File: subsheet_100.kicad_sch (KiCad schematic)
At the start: 12 parts

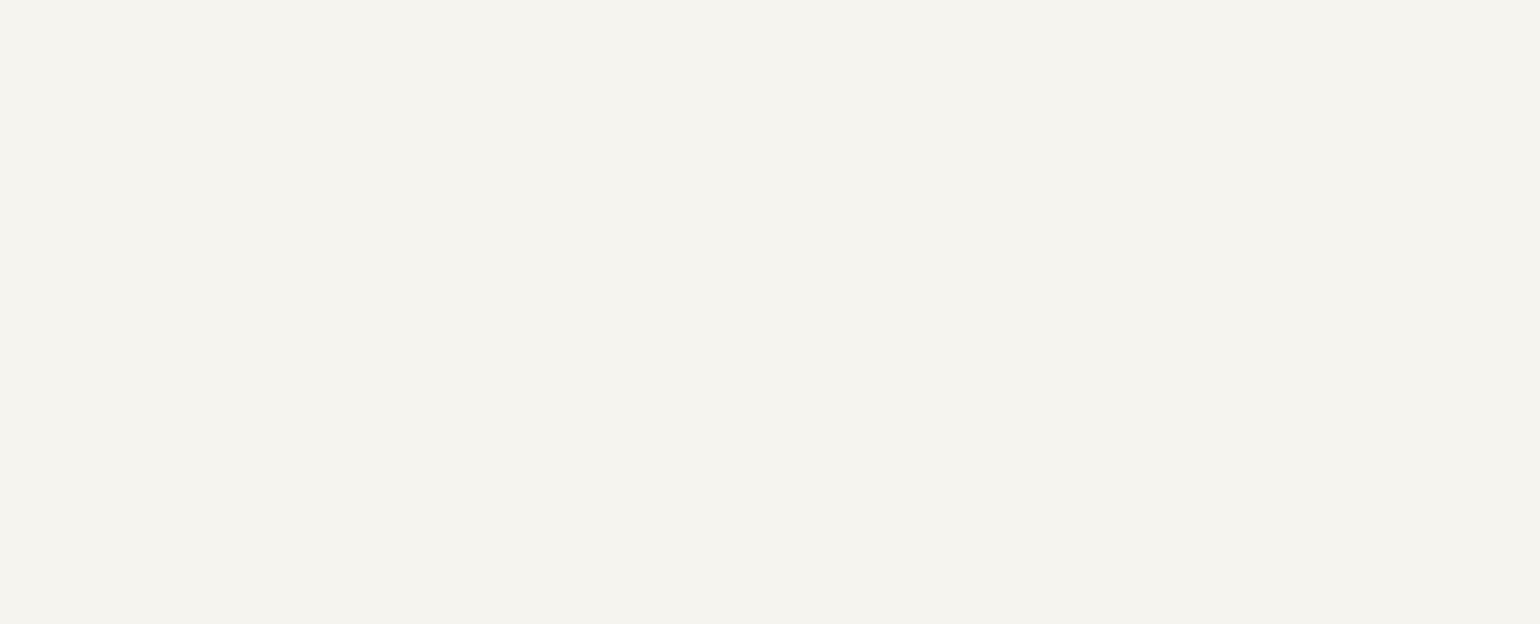
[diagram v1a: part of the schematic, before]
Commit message: bouge I21 vers la page du processeur
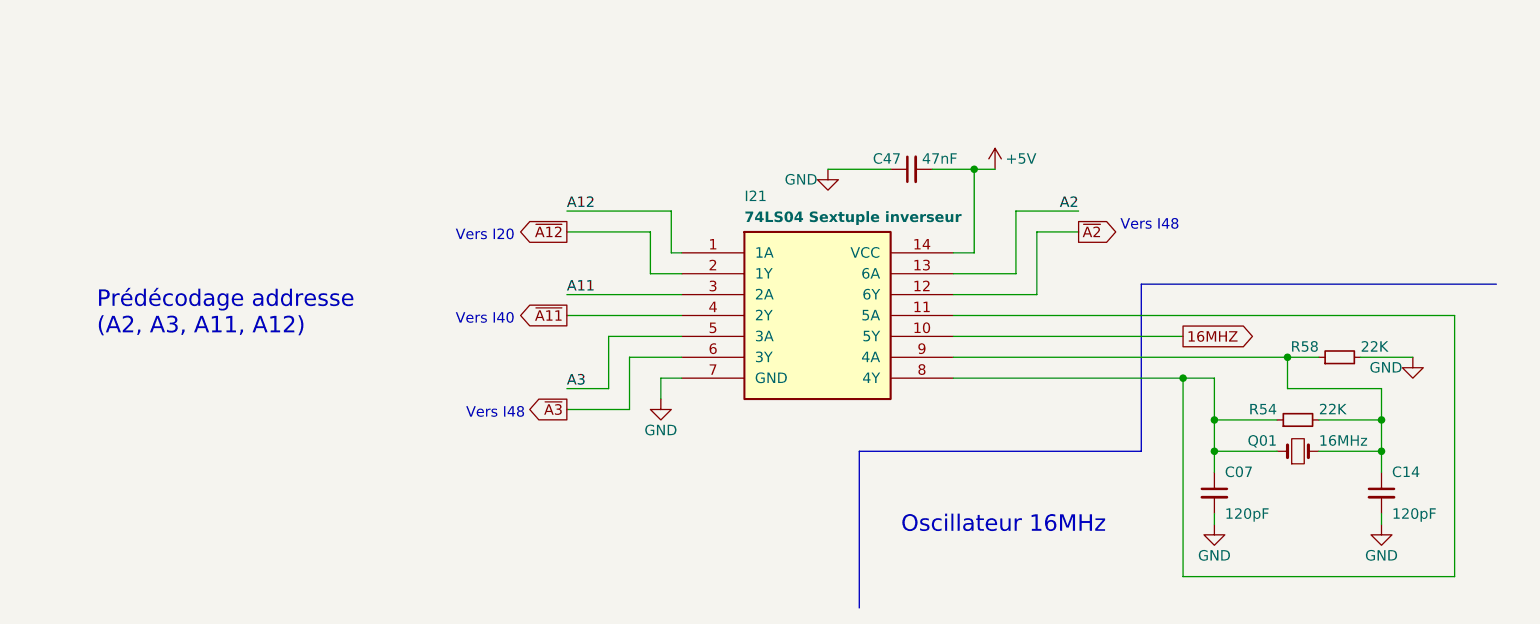
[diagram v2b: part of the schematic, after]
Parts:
- added C07, C14: 120pF, symbol Device:C_Small
- added C47: 47nF, symbol Device:C_Small
- added I21: 74LS04 Sextuple inverseur, Package_DIP:DIP-14_W7.62mm_LongPads, symbol 74x04:74X04_HEX_INVERTER_PHY
- added Q01: 16MHz, symbol Device:Crystal_Small
- added R54, R58: 22K, symbol Device:R_Small
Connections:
- net +5V: now also C47.2, I21.14 (VCC)
- net A11: now also I21.3 (2A)
- net A12: now also I21.1 (1A)
- net A2: now also I21.13 (6A)
- net A3: now also I21.5 (3A)
- net GND: now also C07.2, C14.2, C47.1, I21.7 (GND), R58.2
- new net: C07.1, I21.11 (5A), I21.8 (4Y), Q01.1, R54.1
- new net: C14.1, I21.9 (4A), Q01.2, R54.2, R58.1
- new net 16MHZ: I21.10 (5Y)
- new net ~{A11}: I21.4 (2Y)
- new net ~{A12}: I21.2 (1Y)
- new net ~{A2}: I21.12 (6Y)
- new net ~{A3}: I21.6 (3Y)
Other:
- note added: "Oscillateur 16MHz"
- note added: "Prédécodage addresse (A2, A3, A11, A12)"
- note added: "Vers I20"
- note added: "Vers I40"
- note added: "Vers I48"

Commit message: I16
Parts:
- added C44: 47nF, symbol Device:C_Small
- added I16: 74LS04 Sextuple inverseur, Package_DIP:DIP-14_W7.62mm_LongPads, symbol 74x04:74X04_HEX_INVERTER_PHY
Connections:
- net +5V: now also C44.2, I16.14 (VCC)
- net A14: now also I16.11 (5A)
- net A4: now also I16.3 (2A)
- net A5: now also I16.1 (1A)
- net GND: now also C44.1, I16.7 (GND)
- new net DATA_VALID: I16.6 (3Y)
- new net POINT: I16.12 (6Y)
- new net SYCL: I16.8 (4Y)
- new net ~{A14}: I16.10 (5Y)
- new net ~{A4}: I16.4 (2Y)
- new net ~{A5}: I16.2 (1Y)
- new net ~{DATA_VALID}: I16.5 (3A)
- new net ~{POINT}: I16.13 (6A)
- new net ~{SYCL}: I16.9 (4A)
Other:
- note added: "De I29"
- note added: "De I46"
- note added: "Prédécodage addresse (A4, A5, A14) Cadencement à contre-temps (~{DATA_VALID},~{POINT},SYCL)"
- note added: "Vers I06,I10"
- note added: "Vers I18"
- note added: "Vers I29"

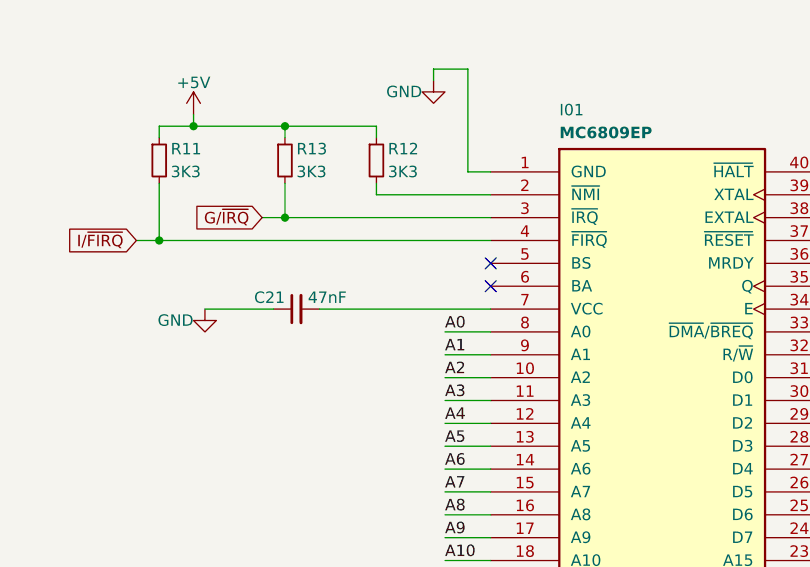
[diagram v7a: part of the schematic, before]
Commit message: fixes DRC : duplicate, designators with '?'
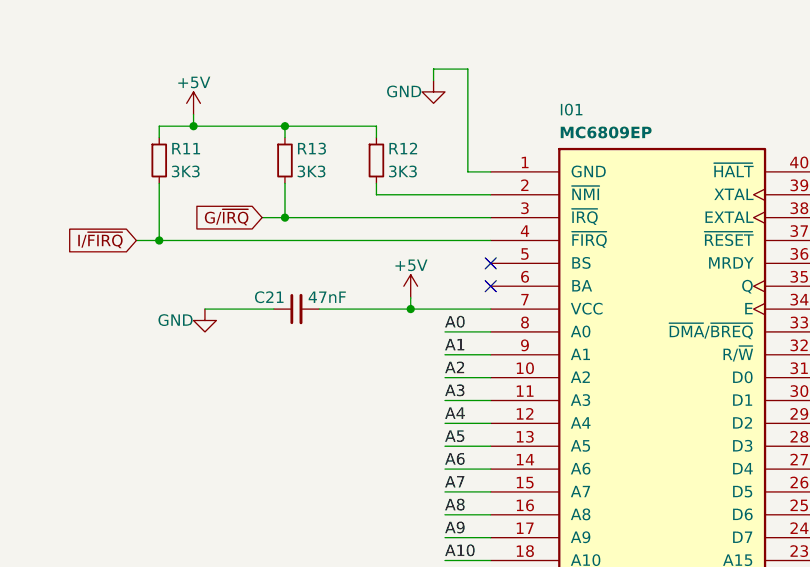
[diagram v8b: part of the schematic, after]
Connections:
- net +5V: now also C21.2, I01.7 (VCC)
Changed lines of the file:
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@@
   (junction (at 147.32 57.15) (diameter 0) (color 0 0 0 0)
+  )
+  (junction (at 58.42 64.77) (diameter 0) (color 0 0 0 0)
   )
   (junction (at 179.07 226.06) (diameter 0) (color 0 0 0 0)
@@
     (stroke (width 0) (type default) (color 0 0 0 0))
   )
+  (wire (pts (xy 58.42 64.77) (xy 67.31 64.77))
+    (stroke (width 0) (type default) (color 0 0 0 0))
+  )
   (wire (pts (xy 152.4 64.77) (xy 152.4 66.04))
     (stroke (width 0) (type default) (color 0 0 0 0))
@@
     (stroke (width 0) (type default) (color 0 0 0 0))
   )
-  (wire (pts (xy 48.26 64.77) (xy 67.31 64.77))
+  (wire (pts (xy 48.26 64.77) (xy 58.42 64.77))
     (stroke (width 0) (type default) (color 0 0 0 0))
   )
@@
   )
   (wire (pts (xy 119.38 76.2) (xy 115.57 76.2))
+    (stroke (width 0) (type default) (color 0 0 0 0))
+  )
+  (wire (pts (xy 58.42 63.5) (xy 58.42 64.77))
     (stroke (width 0) (type default) (color 0 0 0 0))
   )
@@
   (symbol (lib_id "power:+5V") (at 157.48 44.45 0) (unit 1)
     (in_bom yes) (on_board yes)
-    (property "Reference" "#PWR?" (id 0) (at 157.48 48.26 0)
+    (property "Reference" "#PWR0111" (id 0) (at 157.48 48.26 0)
       (effects (font (size 1.27 1.27)) hide)
     )
@@
   (symbol (lib_id "power:+5V") (at 132.08 132.08 0) (unit 1)
     (in_bom yes) (on_board yes)
-    (property "Reference" "#PWR?" (id 0) (at 132.08 135.89 0)
+    (property "Reference" "#PWR0106" (id 0) (at 132.08 135.89 0)
       (effects (font (size 1.27 1.27)) hide)
     )
@@
   (symbol (lib_id "power:+5V") (at 132.08 195.58 0) (unit 1)
     (in_bom yes) (on_board yes)
-    (property "Reference" "#PWR?" (id 0) (at 132.08 199.39 0)
+    (property "Reference" "#PWR0108" (id 0) (at 132.08 199.39 0)
       (effects (font (size 1.27 1.27)) hide)
     )
@@
   (symbol (lib_id "power:+5V") (at 120.65 49.53 0) (unit 1)
     (in_bom yes) (on_board yes)
-    (property "Reference" "#PWR?" (id 0) (at 120.65 53.34 0)
+    (property "Reference" "#PWR0117" (id 0) (at 120.65 53.34 0)
       (effects (font (size 1.27 1.27)) hide)
     )
@@
   (symbol (lib_id "power:GND") (at 60.96 39.37 0) (unit 1)
     (in_bom yes) (on_board yes)
-    (property "Reference" "#PWR?" (id 0) (at 60.96 45.72 0)
+    (property "Reference" "#PWR0113" (id 0) (at 60.96 45.72 0)
       (effects (font (size 1.27 1.27)) hide)
     )
@@
   (symbol (lib_id "power:GND") (at 179.07 238.76 0) (unit 1)
     (in_bom yes) (on_board yes)
-    (property "Reference" "#PWR?" (id 0) (at 179.07 245.11 0)
+    (property "Reference" "#PWR0102" (id 0) (at 179.07 245.11 0)
       (effects (font (size 1.27 1.27)) hide)
     )
@@
   (symbol (lib_id "power:GND") (at 151.13 67.31 0) (unit 1)
     (in_bom yes) (on_board yes)
-    (property "Reference" "#PWR?" (id 0) (at 151.13 73.66 0)
+    (property "Reference" "#PWR0110" (id 0) (at 151.13 73.66 0)
       (effects (font (size 1.27 1.27)) hide)
     )
@@
   (symbol (lib_id "power:GND") (at 111.76 132.08 0) (unit 1)
     (in_bom yes) (on_board yes)
-    (property "Reference" "#PWR?" (id 0) (at 111.76 138.43 0)
+    (property "Reference" "#PWR0107" (id 0) (at 111.76 138.43 0)
       (effects (font (size 1.27 1.27)) hide)
     )
@@
     (pin "1")
     (pin "2")
+  )
+  (symbol (lib_id "power:+5V") (at 58.42 63.5 0) (unit 1)
+    (in_bom yes) (on_board yes)
+    (property "Reference" "#PWR0292" (id 0) (at 58.42 67.31 0)
+      (effects (font (size 1.27 1.27)) hide)
+    )
+    (property "Value" "+5V" (id 1) (at 58.42 59.944 0))
+    (property "Footprint" "" (id 2) (at 58.42 63.5 0)
+      (effects (font (size 1.27 1.27)) hide)
+    )
+    (property "Datasheet" "" (id 3) (at 58.42 63.5 0)
+      (effects (font (size 1.27 1.27)) hide)
+    )
+    (pin "1")
   )
   (symbol (lib_id "74x04:74X04_HEX_INVERTER_PHY") (at 110.49 213.36 0) (unit 1)
@@
   (symbol (lib_id "power:GND") (at 182.88 218.44 0) (unit 1)
     (in_bom yes) (on_board yes)
-    (property "Reference" "#PWR?" (id 0) (at 182.88 224.79 0)
+    (property "Reference" "#PWR0103" (id 0) (at 182.88 224.79 0)
       (effects (font (size 1.27 1.27)) hide)
     )
@@
   (symbol (lib_id "power:GND") (at 35.56 64.77 0) (unit 1)
     (in_bom yes) (on_board yes)
-    (property "Reference" "#PWR?" (id 0) (at 35.56 71.12 0)
+    (property "Reference" "#PWR0112" (id 0) (at 35.56 71.12 0)
       (effects (font (size 1.27 1.27)) hide)
     )
@@
   (symbol (lib_id "power:+5V") (at 34.29 43.18 0) (unit 1)
     (in_bom yes) (on_board yes)
-    (property "Reference" "#PWR?" (id 0) (at 34.29 46.99 0)
+    (property "Reference" "#PWR0114" (id 0) (at 34.29 46.99 0)
       (effects (font (size 1.27 1.27)) hide)
     )
@@
   (symbol (lib_id "power:GND") (at 91.44 160.02 0) (unit 1)
     (in_bom yes) (on_board yes)
-    (property "Reference" "#PWR?" (id 0) (at 91.44 166.37 0)
+    (property "Reference" "#PWR0109" (id 0) (at 91.44 166.37 0)
       (effects (font (size 1.27 1.27)) hide)
     )
@@
   (symbol (lib_id "power:GND") (at 158.75 238.76 0) (unit 1)
     (in_bom yes) (on_board yes)
-    (property "Reference" "#PWR?" (id 0) (at 158.75 245.11 0)
+    (property "Reference" "#PWR0101" (id 0) (at 158.75 245.11 0)
       (effects (font (size 1.27 1.27)) hide)
     )
@@
   (symbol (lib_id "power:GND") (at 120.65 52.07 0) (unit 1)
     (in_bom yes) (on_board yes)
-    (property "Reference" "#PWR?" (id 0) (at 120.65 58.42 0)
+    (property "Reference" "#PWR0115" (id 0) (at 120.65 58.42 0)
       (effects (font (size 1.27 1.27)) hide)
     )
@@
   (symbol (lib_id "power:GND") (at 111.76 195.58 0) (unit 1)
     (in_bom yes) (on_board yes)
-    (property "Reference" "#PWR?" (id 0) (at 111.76 201.93 0)
+    (property "Reference" "#PWR0105" (id 0) (at 111.76 201.93 0)
       (effects (font (size 1.27 1.27)) hide)
     )
@@
   (symbol (lib_id "power:GND") (at 91.44 223.52 0) (unit 1)
     (in_bom yes) (on_board yes)
-    (property "Reference" "#PWR?" (id 0) (at 91.44 229.87 0)
+    (property "Reference" "#PWR0104" (id 0) (at 91.44 229.87 0)
       (effects (font (size 1.27 1.27)) hide)
     )
@@
   (symbol (lib_id "power:+5V") (at 137.16 71.12 0) (unit 1)
     (in_bom yes) (on_board yes)
-    (property "Reference" "#PWR?" (id 0) (at 137.16 74.93 0)
-      (effects (font (size 1.27 1.27)) hide)
-    )
+    (property "Reference" "#PWR0116" (id 0) (at 137.16 74.93 0)
+      (effects (font (size 1.27 1.27)) hide)
+    )
